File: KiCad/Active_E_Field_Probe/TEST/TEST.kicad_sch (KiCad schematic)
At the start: 27 parts

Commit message: AAAAAAAAAAAHHHHH
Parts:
- added C10, C8: {C_s}, symbol SLiCAP:C
- added C11, C9: {0.5*C_s}, symbol SLiCAP:C
- added M5: ~, symbol SLiCAP:M
- added N4: ~, symbol SLiCAP:N
- added R4 (x2), R5 (x2): 50, symbol SLiCAP:R
- added V1 (x2): {V_in}, symbol SLiCAP:V
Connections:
- net 0: now also M5.3 (S), M5.4 (B), N4.2 (outN), N4.4 (inN), R4.2, R5.2, V1.2 (n), V1.2 (n)
- new net: C8.1, V1.1 (p)
- new net: C9.2, M5.1 (D), R4.1
- new net: C8.2, C9.1, M5.2 (G)
- new net: C11.2, N4.1 (outP), R5.1
- new net: C10.2, C11.1, N4.3 (inp)
- new net: C10.1, V1.1 (p)
- new net out: R4.1, R4.2, R5.1, R5.2

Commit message: 01-10 sesh
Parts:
- removed C8: {C_s}, symbol SLiCAP:C
- removed C9: {0.5*C_s}, symbol SLiCAP:C
- removed M5: ~, symbol SLiCAP:M
- removed R4 (x2): 50, symbol SLiCAP:R
- removed V1: {V_in}, symbol SLiCAP:V
- added A1, A2, A3: ~, symbol SLiCAP:Command
- added C12, C14, C16: {C_s}, symbol SLiCAP:C
- added C13, C15, C17: {0.5*C_s}, symbol SLiCAP:C
- added M6, M7, M8: ~, symbol SLiCAP:M
- added R10, R11, R6, R7, R8, R9: 50, symbol SLiCAP:R
- added V1 (x2), V3: {V_in}, symbol SLiCAP:V
- added X2: ~, symbol SLiCAP:XMV
- renumbered V3 to V1
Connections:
- net 0: now also M6.3 (S), M6.4 (B), M7.3 (S), M7.4 (B), M8.3 (S), M8.4 (B), R11.2, R7.2, R9.2, V1.2 (n), V1.2 (n), V3.2 (n), X2.3 (S), X2.B (4)
- net out: now also R10.2, R11.1, R6.2, R7.1, R8.2, R9.1
- new net: C16.2, C17.1, M8.2 (G)
- new net: C17.2, M8.1 (D), R10.1
- new net: C14.1, V3.1 (p)
- new net: C14.2, C15.1, X2.2 (G)
- new net: C12.2, C13.1, M6.2 (G), M7.2 (G)
- new net: C15.2, R8.1, X2.1 (D)
- new net: C16.1, V1.1 (p)
- new net: C12.1, V1.1 (p)
- new net LGref: C13.2, M6.1 (D), M7.1 (D), R6.1
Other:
- moved on the sheet: C1, C10, C11, C2, C3, C4, C5, C6, C7, D1, D2, D3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

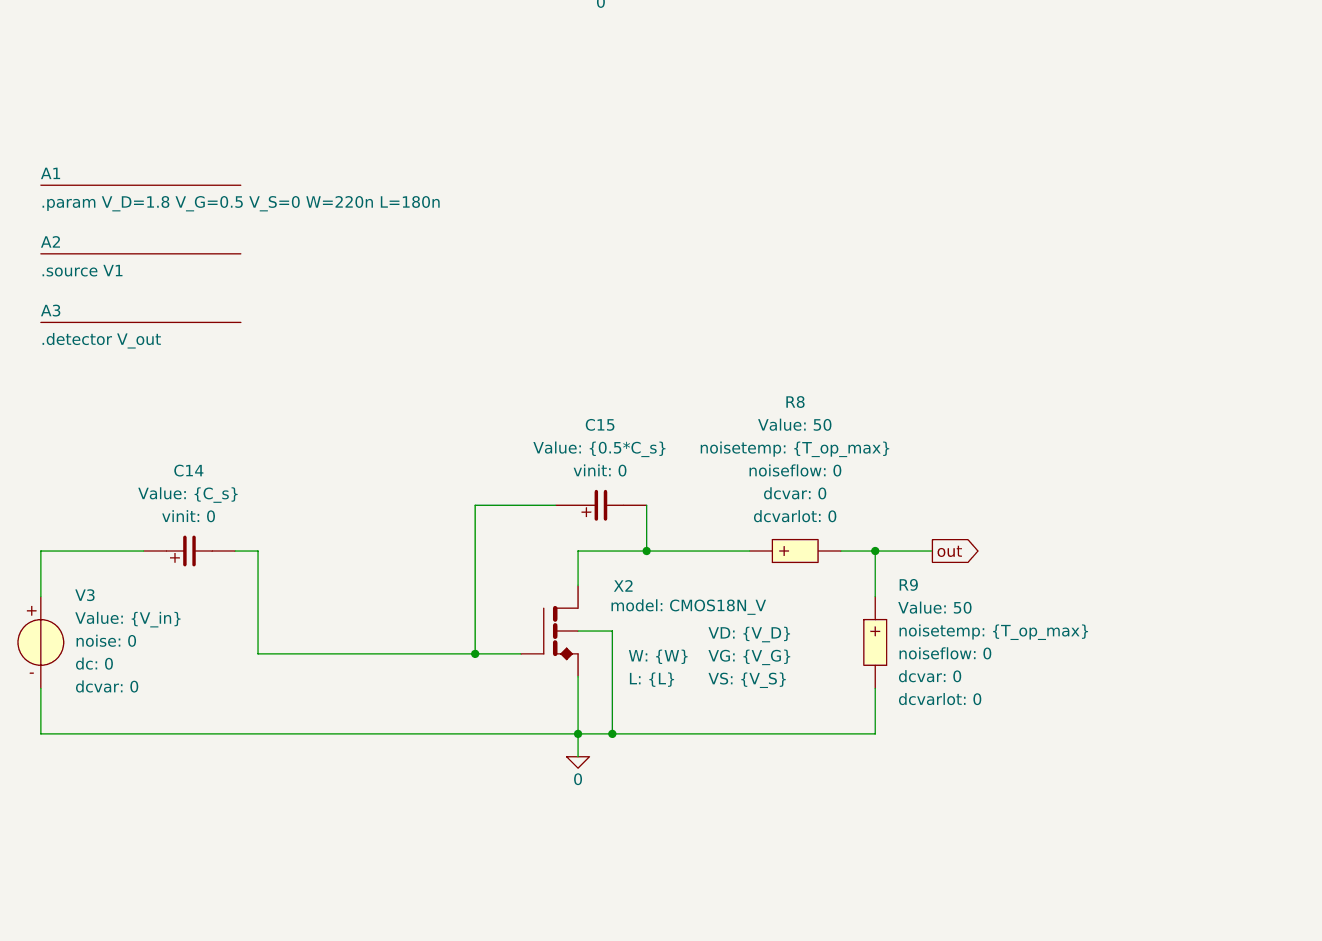
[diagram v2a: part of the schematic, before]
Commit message: Split python files
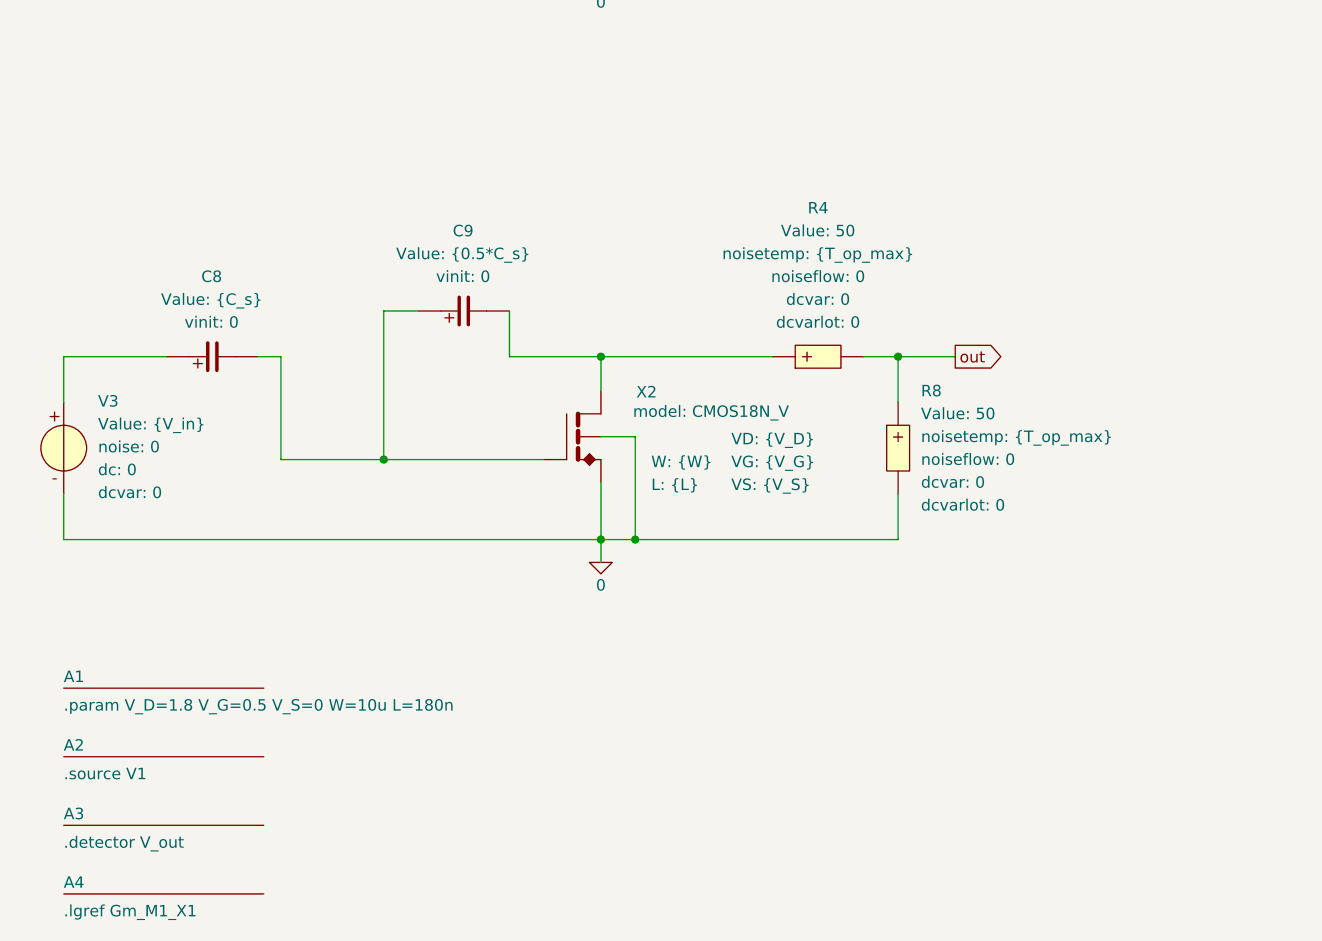
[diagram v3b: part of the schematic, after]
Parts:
- removed C14: {C_s}, symbol SLiCAP:C
- removed C15: {0.5*C_s}, symbol SLiCAP:C
- removed R9: 50, symbol SLiCAP:R
- added A4: ~, symbol SLiCAP:Command
- added C8: {C_s}, symbol SLiCAP:C
- added C9: {0.5*C_s}, symbol SLiCAP:C
- added R4: 50, symbol SLiCAP:R
- A1: command .param V_D=1.8 V_G=0.5 V_S=0 W=220n L=180n -> .param V_D=1.8 V_G=0.5 V_S=0 W=10u L=180n
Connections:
- net 0: now also R8.2
- net out: now also R8.1, R4.2; no longer R8.2
- net at V3.1 (p): now also C8.1
- net at X2.2 (G): now also C8.2, C9.1
- net at X2.1 (D): now also C9.2, R4.1; no longer R8.1
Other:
- moved on the sheet: A1, A2, A3

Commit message: 2 stage
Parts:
- added C14, C18, C20, C22, C24: {C_s}, symbol SLiCAP:C
- added C15, C19, C21, C23, C25: {0.4*C_s}, symbol SLiCAP:C
- added R12, R13, R14, R15, R16, R17, R18, R19, R9 (x2): 50, symbol SLiCAP:R
- added V4, V5, V6, V7, V8: {V_in}, symbol SLiCAP:V
- added X10, X11, X12, X3, X4, X5, X7, X8, X9: ~, symbol SLiCAP:XM
- added X6: ~, symbol SLiCAP:XMPN
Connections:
- net 0: now also R13.2, R15.2, R17.2, R19.2, R9.2, V4.2 (n), V5.2 (n), V6.2 (n), V7.2 (n), V8.2 (n), X10.3 (S), X10.4 (B), X11.4 (B), X12.1 (D), X12.4 (B), X3.3 (S), X3.4 (B), X4.3 (S), X4.4 (B), X5.3 (S), X5.4 (B), X6.3 (S), X6.4 (B), X7.3 (S), X7.4 (B), X8.3 (S), X8.4 (B), X9.3 (S), X9.4 (B)
- new net: C22.2, C23.1, X7.2 (G)
- new net: X7.1 (D), X8.2 (G), X9.2 (G)
- new net: X10.1 (D), X11.2 (G)
- new net: X11.3 (S), X12.2 (G)
- new net: C18.1, V5.1 (p)
- new net: C18.2, C19.1, X4.2 (G), X5.2 (G)
- new net: C22.1, V7.1 (p)
- new net: C24.2, C25.1, X10.2 (G)
- new net: C14.1, V4.1 (p)
- new net: C14.2, C15.1, X3.2 (G)
- new net: C20.2, C21.1, X6.2 (G)
- new net: C24.1, V8.1 (p)
- new net: C20.1, V6.1 (p)
- new net Amp_out: C15.2, C19.2, C21.2, C23.2, C25.2, R12.1, R14.1, R16.1, R18.1, R9.1, X11.1 (D), X12.3 (S), X3.1 (D), X4.1 (D), X5.1 (D), X6.1 (D), X8.1 (D), X9.1 (D)
- new net vo: R12.2, R13.1, R14.2, R15.1, R16.2, R17.1, R18.2, R19.1, R9.1, R9.2

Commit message: something
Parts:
- X7: ID {ID_N} -> {ID1_N}; L {L_N} -> {L1_N}; W {W_N} -> {W1_N}
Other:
- moved on the sheet: C22, C23, R16, R17

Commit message: Loopgain Fucked
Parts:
- added C26, C28: {C_s}, symbol SLiCAP:C
- added C27, C29: {0.4*C_s}, symbol SLiCAP:C
- added R20, R21, R22, R23: 50, symbol SLiCAP:R
- added V10, V9: {V_in}, symbol SLiCAP:V
- added X13, X16: ~, symbol SLiCAP:XMD
- added X14, X15: ~, symbol SLiCAP:XM
- added X17: ~, symbol SLiCAP:XMPN
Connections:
- net 0: now also R21.2, R23.2, V10.2 (n), V9.2 (n), X13.4 (G2), X14.3 (S), X14.4 (B), X15.3 (S), X15.4 (B), X16.4 (G2), X17.3 (S), X17.4 (B)
- net Amp_out: now also C27.2, C29.2, R20.1, X14.1 (D), X15.1 (D)
- net vo: now also R20.2, R21.1, R22.2, R23.1
- new net: C28.2, C29.1, X16.3 (G1)
- new net: C28.1, V10.1 (p)
- new net: R22.1, X17.1 (D)
- new net: X16.2 (D2), X17.2 (G)
- new net: C26.1, V9.1 (p)
- new net: C26.2, C27.1, X13.3 (G1)
- new net: X13.2 (D2), X14.2 (G), X15.2 (G)

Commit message: NoiseStuff
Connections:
- net Amp_out: now also R22.1, X17.1 (D)

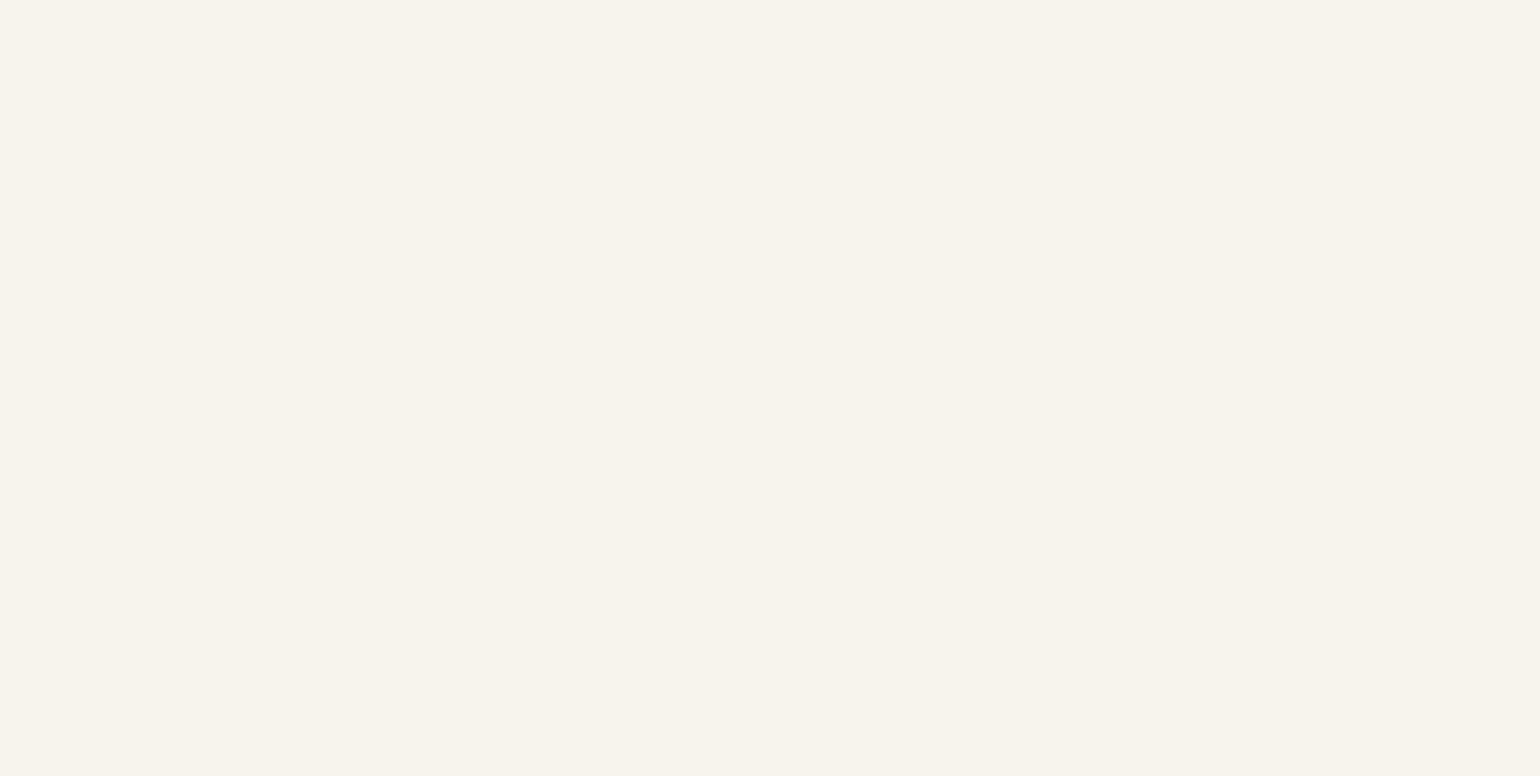
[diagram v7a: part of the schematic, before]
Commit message: cleaned up code and pages
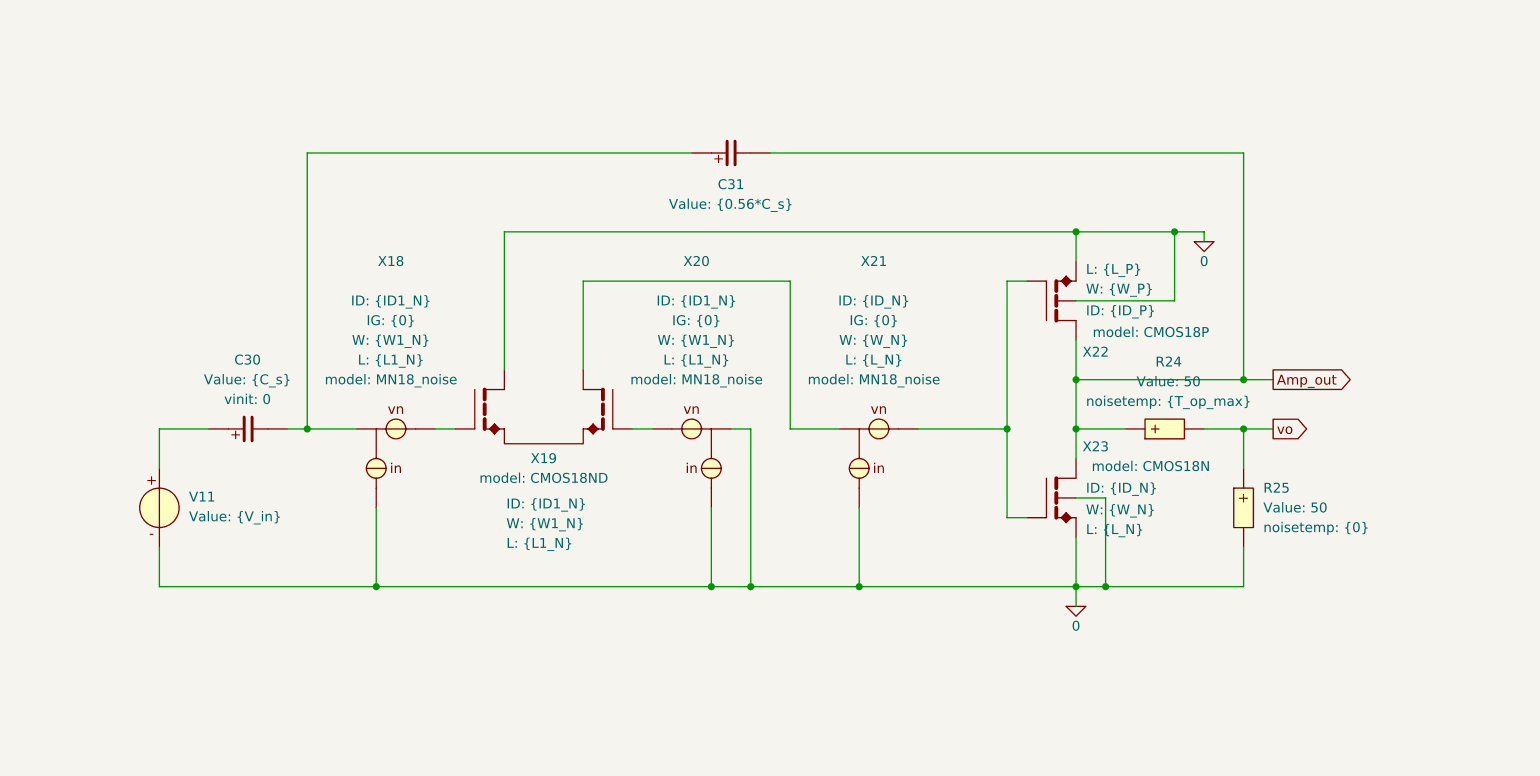
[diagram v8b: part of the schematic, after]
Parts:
- added C30: {C_s}, symbol SLiCAP:C
- added C31: {0.56*C_s}, symbol SLiCAP:C
- added R24, R25: 50, symbol SLiCAP:R
- added V11: {V_in}, symbol SLiCAP:V
- added X18, X20, X21: ~, symbol SLiCAP:M_noise
- added X19: ~, symbol SLiCAP:XMD
- added X22, X23: ~, symbol SLiCAP:XM
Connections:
- net 0: now also R25.2, V11.2 (n), X18.2 (comm), X19.1 (D1), X20.1 (ext), X20.2 (comm), X21.2 (comm), X22.3 (S), X22.4 (B), X23.3 (S), X23.4 (B)
- net Amp_out: now also C31.2, R24.1, X22.1 (D), X23.1 (D)
- net vo: now also R24.2, R25.1
- new net: C30.2, C31.1, X18.1 (ext)
- new net: X21.3 (int), X22.2 (G), X23.2 (G)
- new net: C30.1, V11.1 (p)
- new net: X19.2 (D2), X21.1 (ext)
- new net: X18.3 (int), X19.3 (G1)
- new net: X19.4 (G2), X20.3 (int)
